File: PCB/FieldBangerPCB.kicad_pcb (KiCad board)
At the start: 2 copper layers, 185 x 50 mm, 11 parts, among them J1 8P8C, SW1 SW_SPST, SW2 SW_SPST, SW3 SW_SPST, SW4 SW_SPST, SW5 SW_SPST, SW6 SW_SPST, SW7 SW_SPST, SW8 SW_SPST, SW9 SW_SPST

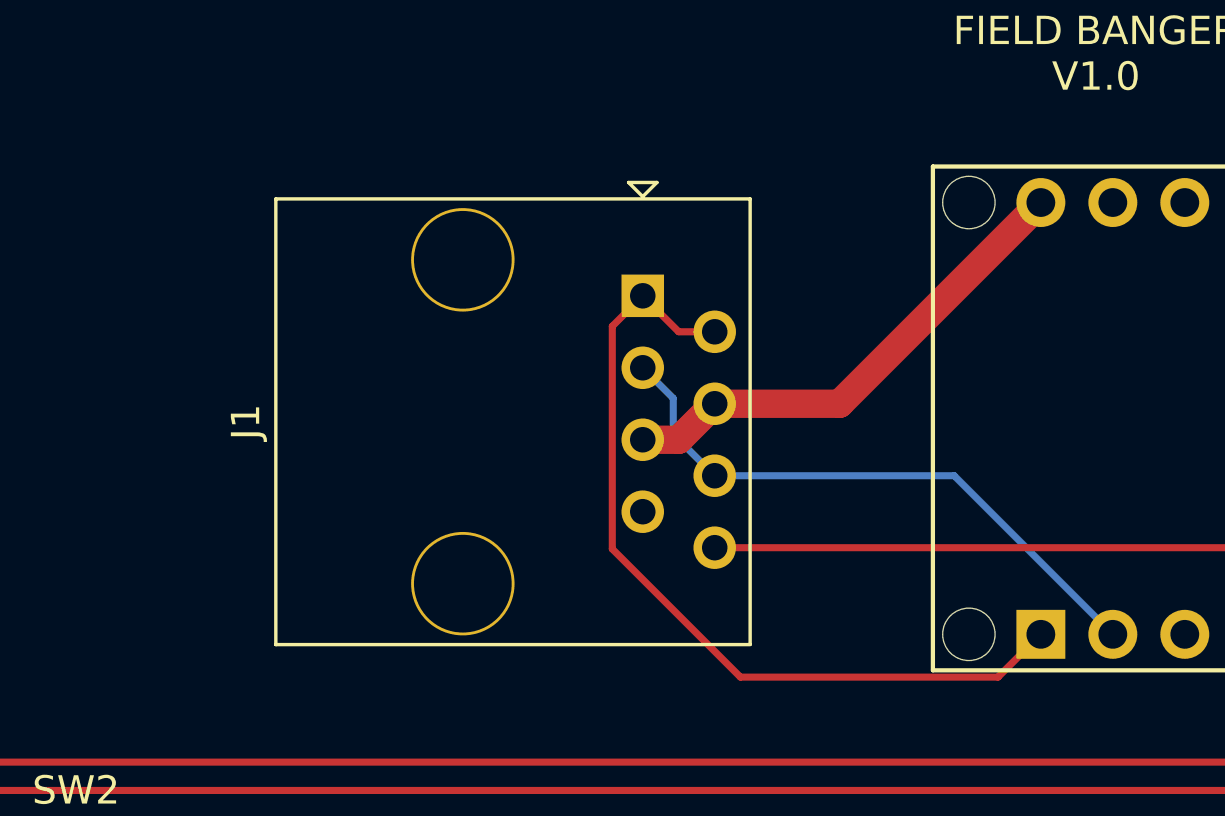
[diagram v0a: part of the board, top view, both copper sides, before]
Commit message: added power cap
added 180uF cap to power input to help with power filtering.
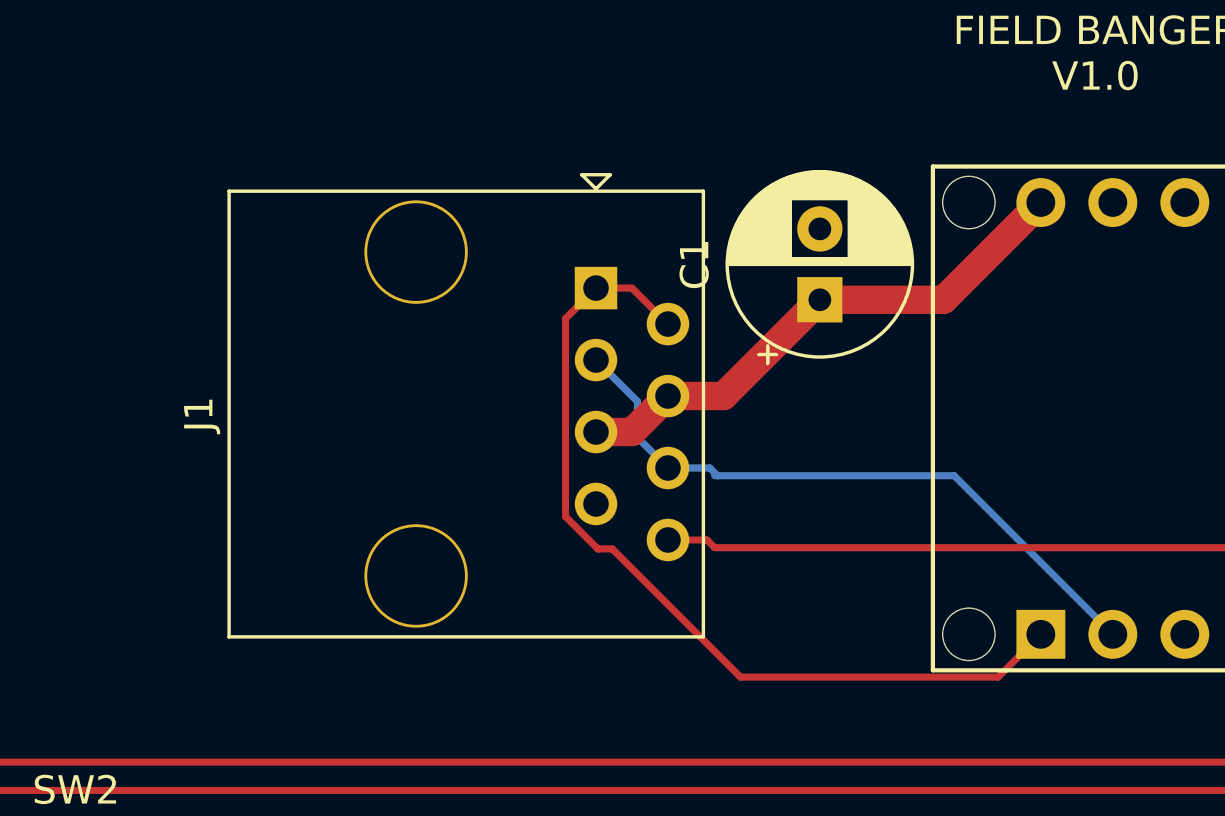
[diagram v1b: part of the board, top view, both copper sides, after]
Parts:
- added C1: C_Polarized_Small_US, Capacitor_THT:CP_Radial_D6.3mm_P2.50mm, F.Cu at (113.2, 41.7)
- moved J1 1.67 mm to (105.3, 41.3)
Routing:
- net Net-(J1-Pad3): track 21.2 -> 23.1 mm
- net Net-(J1-Pad8): track 52.1 -> 53.9 mm
- net +12V: track 17.5 -> 19.1 mm
- net Net-(J1-Pad1): track 30.1 -> 31.3 mm
